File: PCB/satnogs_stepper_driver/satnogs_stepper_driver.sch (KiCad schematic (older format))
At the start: 16 parts, among them P1 CONN_01X18, P2 CONN_01X02, P3 MOTOR 1, P4 MOTOR 2, U1 POLOLU_A4988, U2 POLOLU_A4988

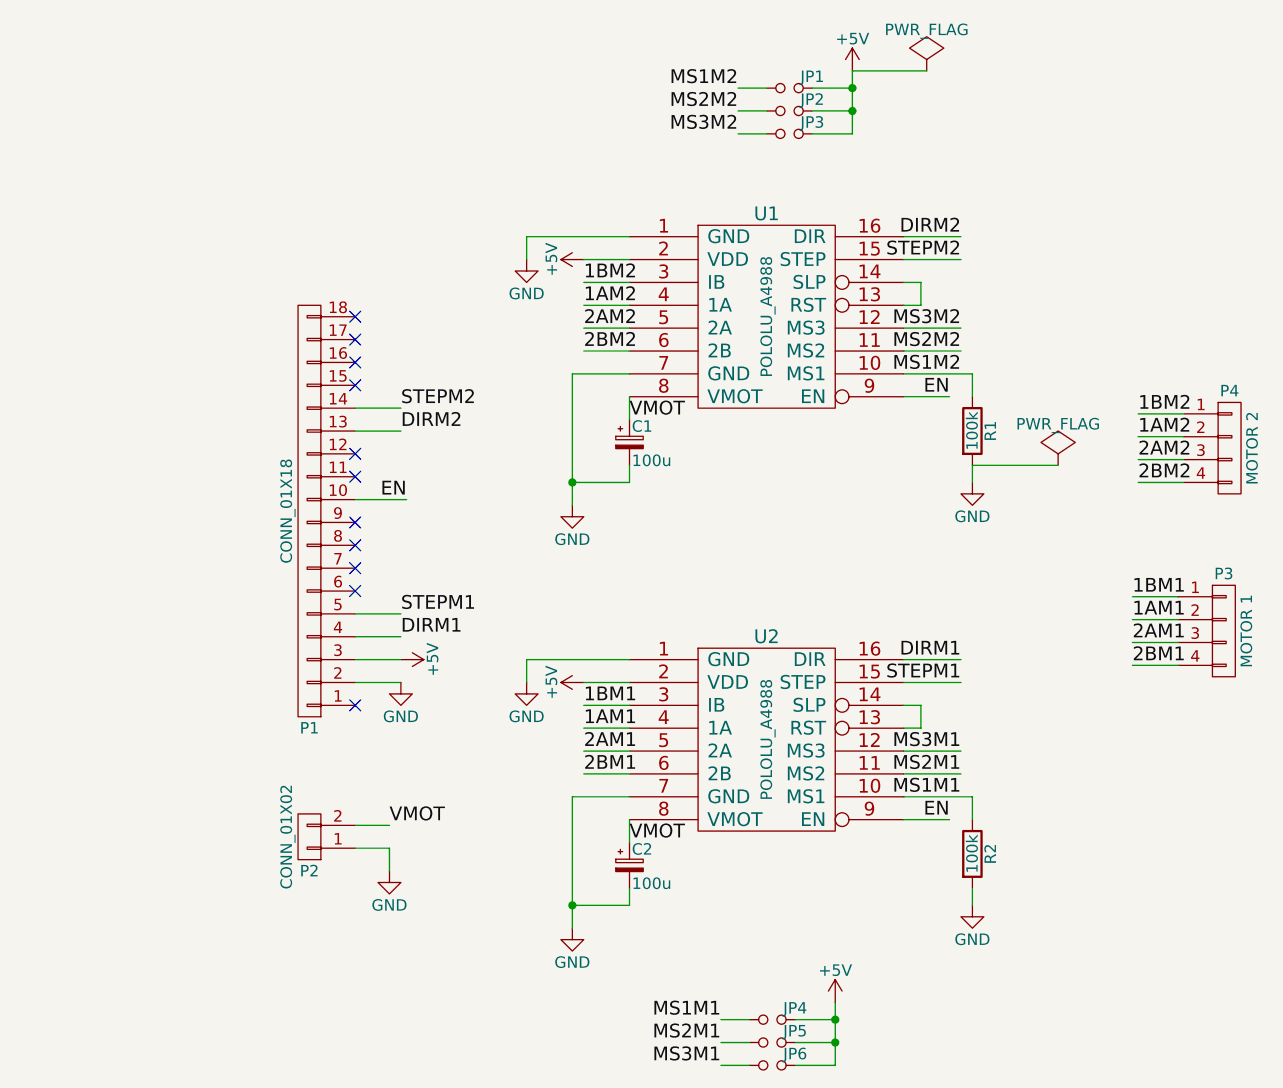
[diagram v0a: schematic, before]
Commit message: Update stepper driver PCB, add BOM.
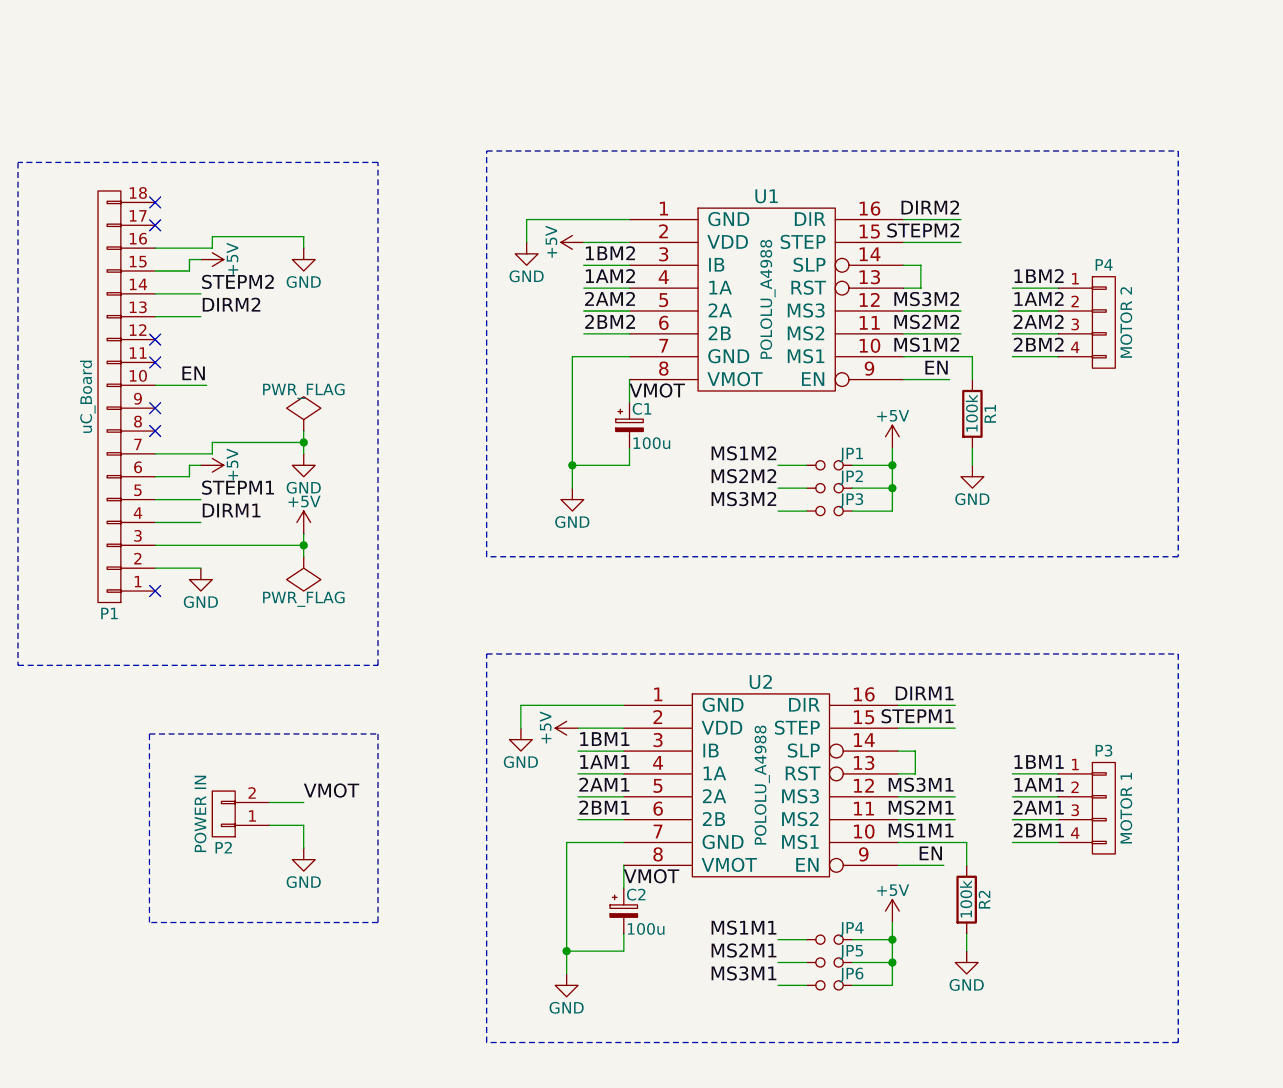
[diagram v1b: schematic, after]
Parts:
- P1: value CONN_01X18 -> uC_Board
- P2: value CONN_01X02 -> POWER IN
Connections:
- net +5V: now also P1.15 (P15), P1.6 (P6)
- net GND: now also P1.16 (P16), P1.7 (P7)
- no-connect marks 11 -> 7
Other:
- moved on the sheet: C1, C2, JP1, JP2, JP3, JP4, JP5, JP6, P1, P2, P3, P4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

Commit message: Small fixes.
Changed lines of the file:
@@
 Wire Notes Line
 	4825 5375 4825 3675
+Text Label 2780 1530 0    60   ~ 0
+ControllerHeader
+Text Label 4830 1480 0    60   ~ 0
+Motor1
+Text Label 4830 3680 0    60   ~ 0
+Motor2
+Text Label 3350 4020 0    60   ~ 0
+PowerIn
 $EndSCHEMATC
